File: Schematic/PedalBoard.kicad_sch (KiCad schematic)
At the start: 10 parts, among them U1 SC0918, U2 ADS1115IDGST, U3 ADS1115IDGST, U4 THB001P

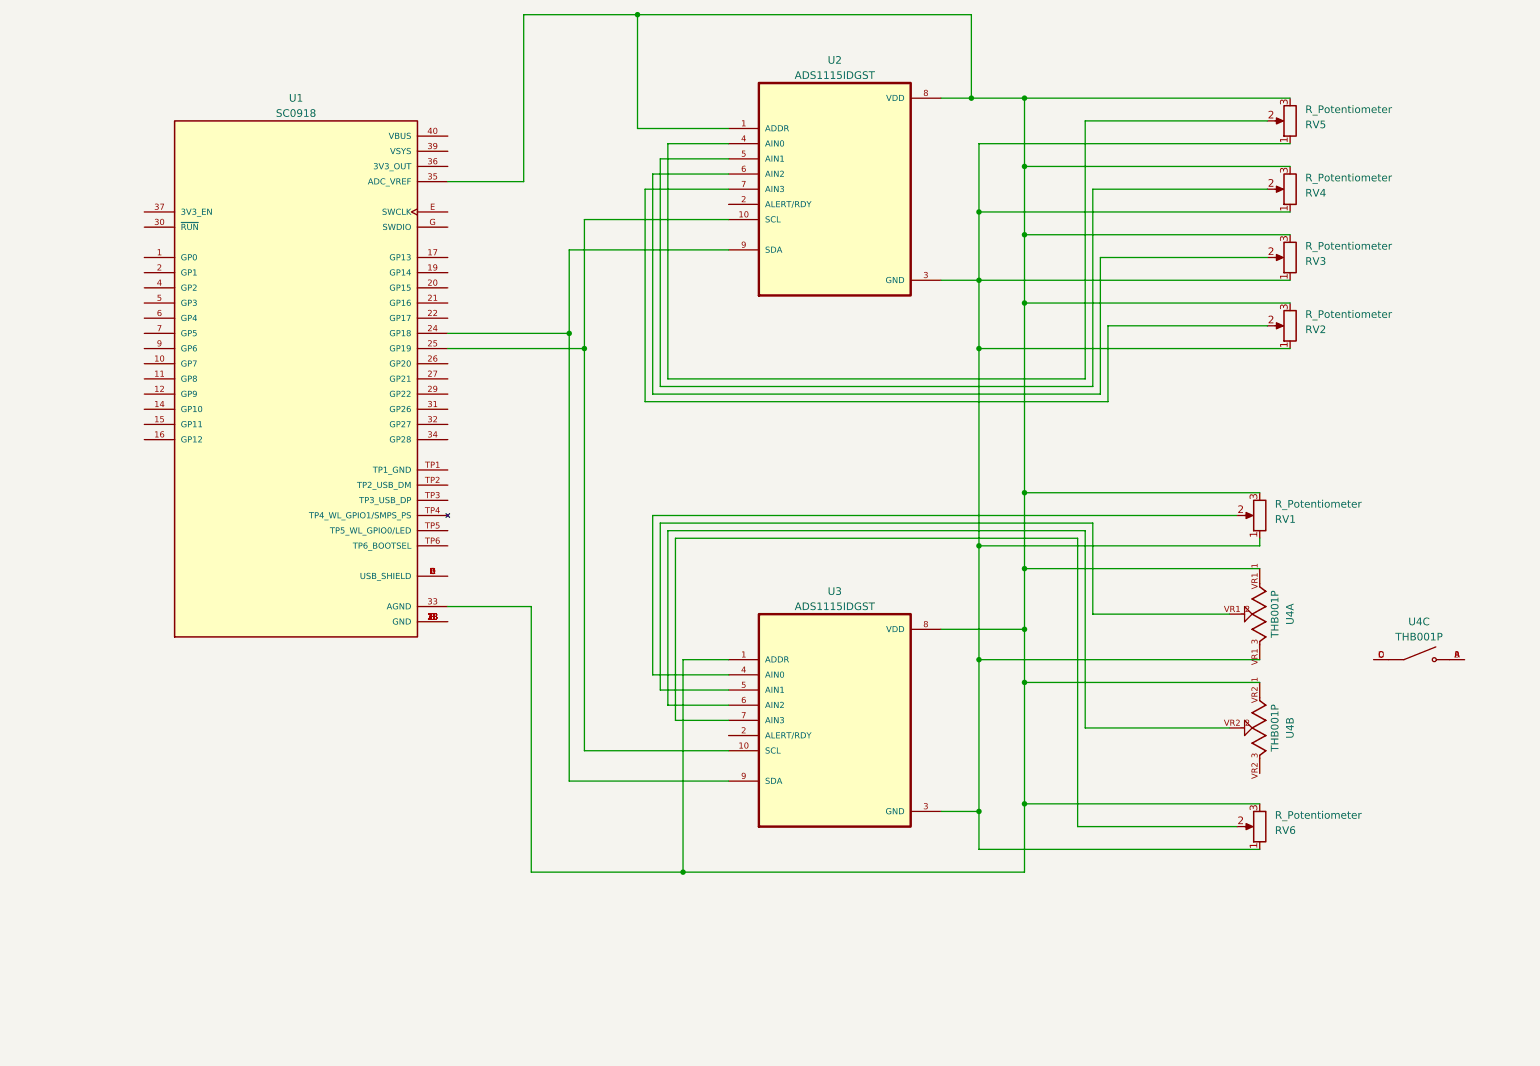
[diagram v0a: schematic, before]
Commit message: Added Leds
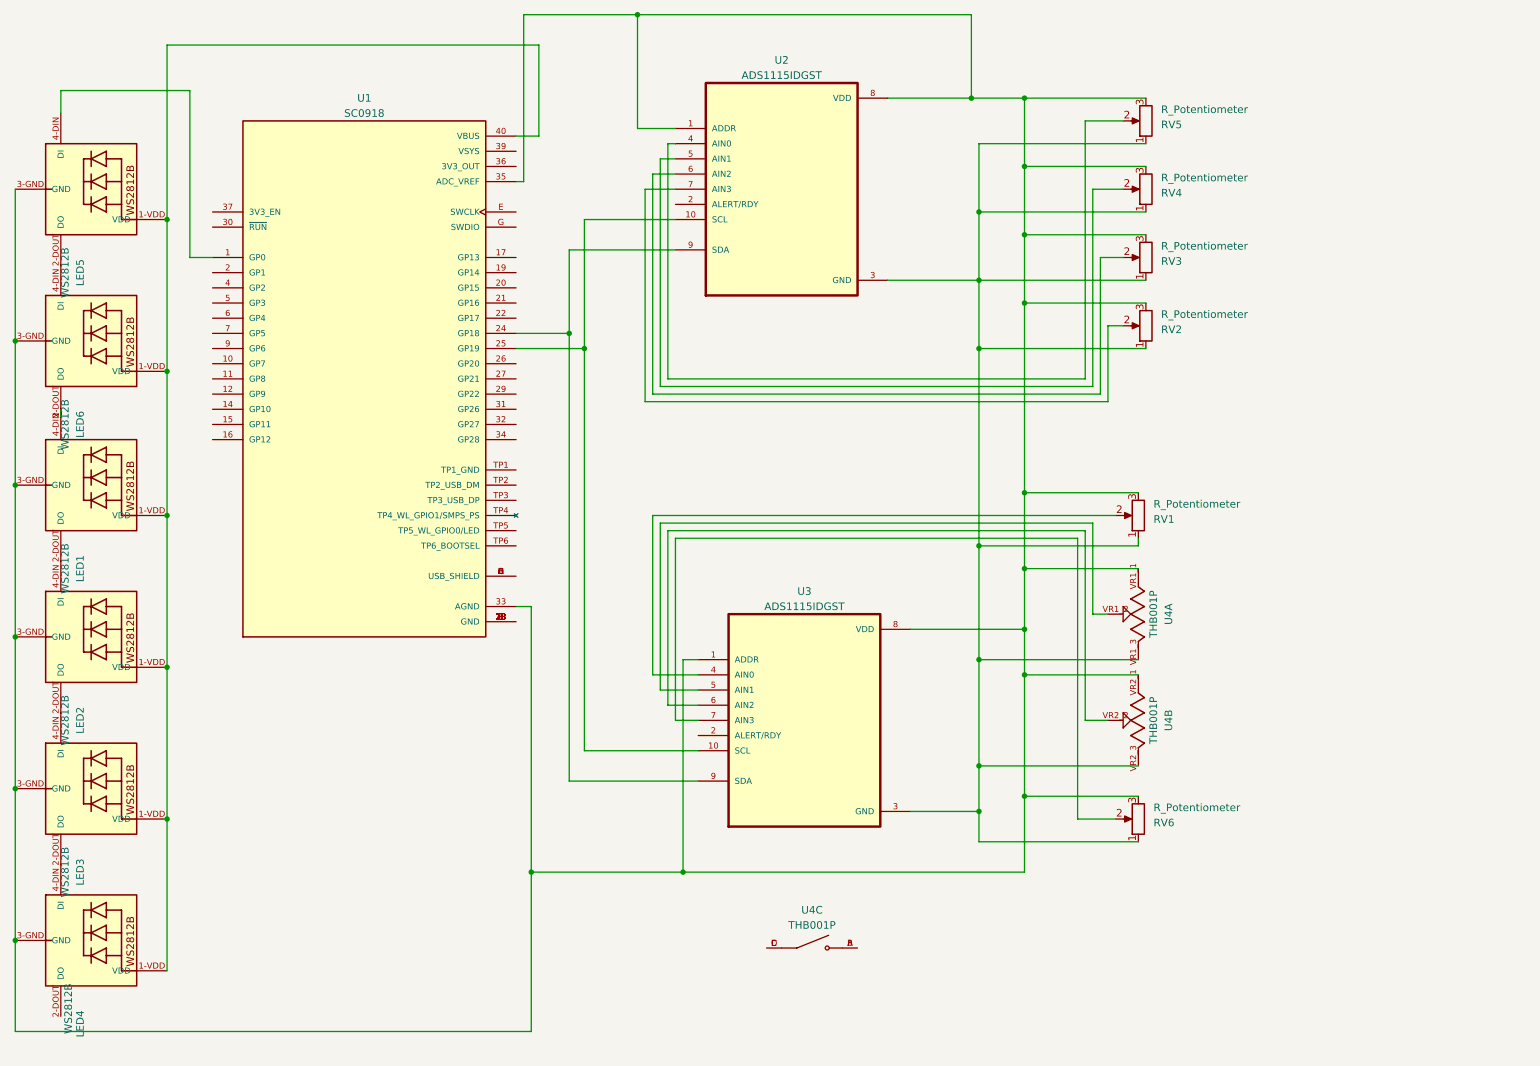
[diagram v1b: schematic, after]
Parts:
- added LED1, LED2, LED3, LED4, LED5, LED6: WS2812B, symbol WS2812B:WS2812B
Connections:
- net at RV1.3, RV2.3, RV3.3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: now also LED1.3-GND (GND), LED2.3-GND (GND), LED3.3-GND (GND), LED4.3-GND (GND), LED5.3-GND (GND), LED6.3-GND (GND)
- net at RV1.1, RV2.1, RV3.1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: now also U4.VR2_3
- net at U1.1 (GP0): now also LED5.4-DIN (DI)
- net at U1.40 (VBUS): now also LED1.1-VDD (VDD), LED2.1-VDD (VDD), LED3.1-VDD (VDD), LED4.1-VDD (VDD), LED5.1-VDD (VDD), LED6.1-VDD (VDD)
- new net: LED5.2-DOUT (DO), LED6.4-DIN (DI)
- new net: LED3.2-DOUT (DO), LED4.4-DIN (DI)
- new net: LED1.2-DOUT (DO), LED2.4-DIN (DI)
- new net: LED1.4-DIN (DI), LED6.2-DOUT (DO)
- new net: LED2.2-DOUT (DO), LED3.4-DIN (DI)
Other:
- moved on the sheet: RV1, RV2, RV3, RV4, RV5, RV6, U1, U2, U3, U4A, U4B, U4C

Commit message: Added footswitch to schematic
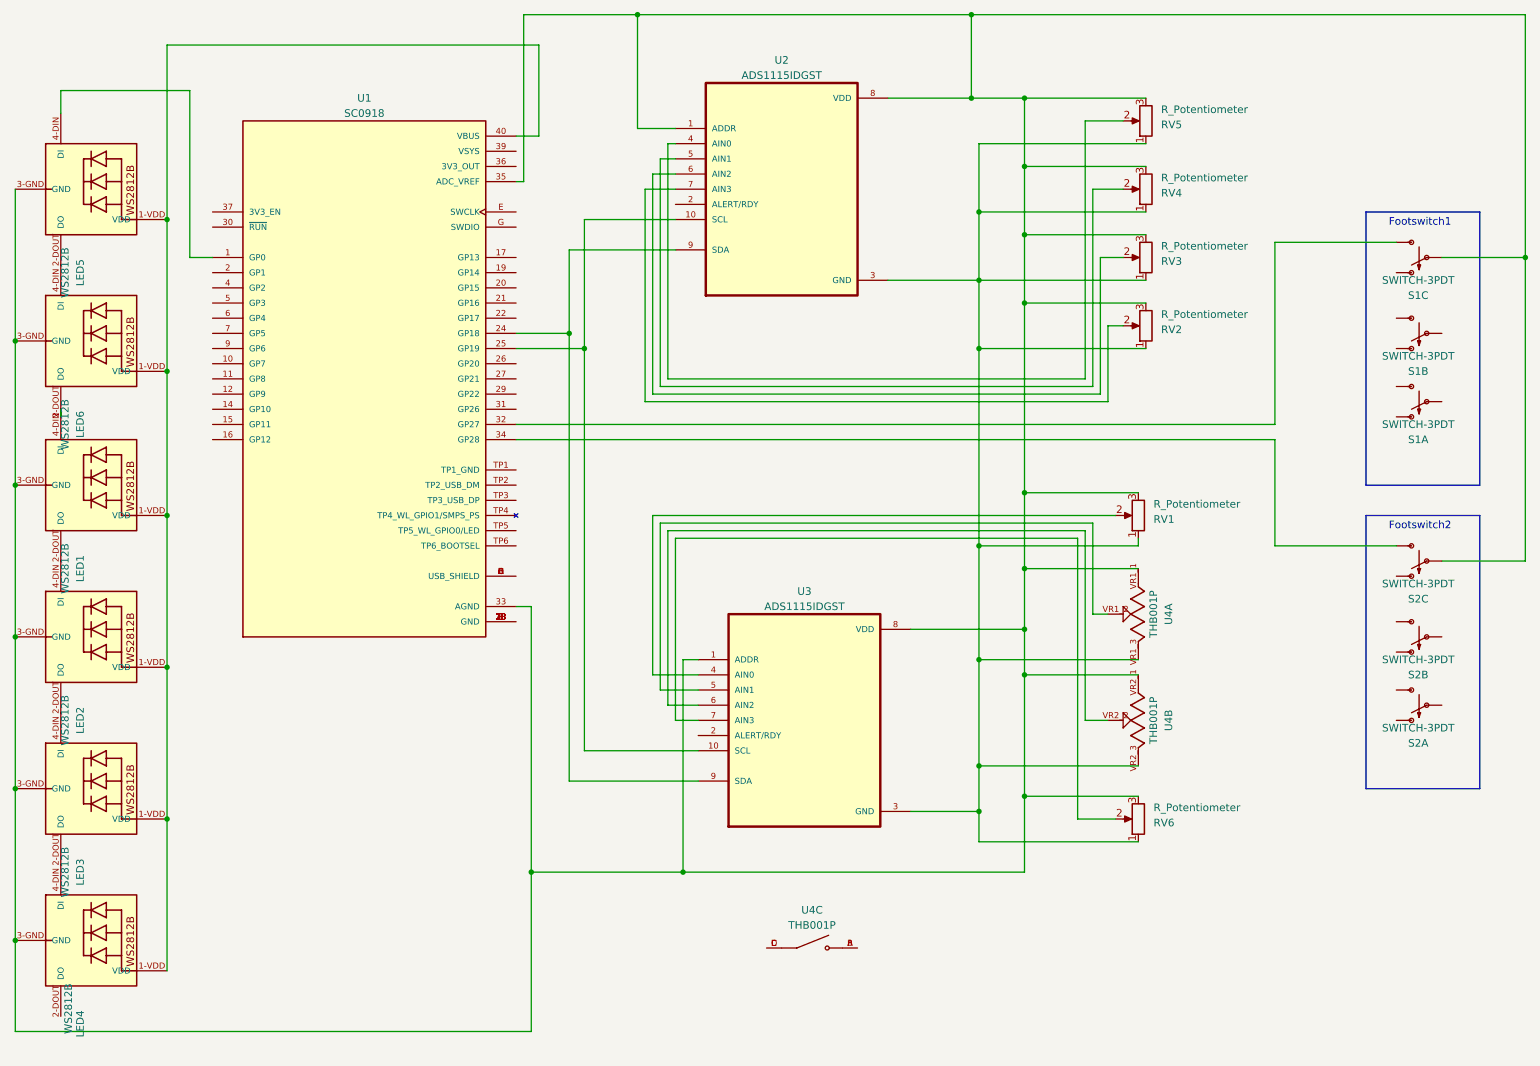
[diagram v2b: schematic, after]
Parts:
- added S1, S2: SWITCH-3PDT, STOMP-SWITCH-3PDT, symbol SparkFun-Electromechanical:SWITCH-3PDT
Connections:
- net at LED1.3-GND (GND), LED2.3-GND (GND), LED3.3-GND (GND)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: now also S1.P$8 (P), S2.P$8 (P)
- net at U1.32 (GP27): now also S1.P$9 (S)
- net at U1.34 (GP28): now also S2.P$9 (S)
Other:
- note added: "Footswitch1"
- note added: "Footswitch2"
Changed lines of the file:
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@@
   (junction (at 191.77 45.72) (diameter 0) (color 0 0 0 0)
   )
+  (junction (at 182.88 20.32) (diameter 0) (color 0 0 0 0)
+  )
   (junction (at 22.86 99.06) (diameter 0) (color 0 0 0 0)
   )
@@
   (junction (at 184.15 53.34) (diameter 0) (color 0 0 0 0)
   )
+  (junction (at 275.59 60.96) (diameter 0) (color 0 0 0 0)
+  )
   (wire (pts (xy 191.77 34.29) (xy 212.09 34.29))
     (stroke (width 0) (type default))
@@
     (stroke (width 0) (type default))
   )
+  (wire (pts (xy 275.59 20.32) (xy 275.59 60.96))
+    (stroke (width 0) (type default))
+  )
   (wire (pts (xy 172.72 153.67) (xy 184.15 153.67))
     (stroke (width 0) (type default))
   )
+  (wire (pts (xy 233.68 91.44) (xy 106.68 91.44))
+    (stroke (width 0) (type default))
+  )
   (wire (pts (xy 200.66 107.95) (xy 200.66 154.94))
     (stroke (width 0) (type default))
@@
     (stroke (width 0) (type default))
   )
+  (wire (pts (xy 233.68 88.9) (xy 106.68 88.9))
+    (stroke (width 0) (type default))
+  )
+  (wire (pts (xy 233.68 109.22) (xy 233.68 91.44))
+    (stroke (width 0) (type default))
+  )
   (wire (pts (xy 191.77 130.81) (xy 210.82 130.81))
     (stroke (width 0) (type default))
@@
     (stroke (width 0) (type default))
   )
+  (wire (pts (xy 182.88 20.32) (xy 275.59 20.32))
+    (stroke (width 0) (type default))
+  )
   (wire (pts (xy 106.68 40.64) (xy 110.49 40.64))
     (stroke (width 0) (type default))
@@
     (stroke (width 0) (type default))
   )
+  (wire (pts (xy 254 109.22) (xy 233.68 109.22))
+    (stroke (width 0) (type default))
+  )
   (wire (pts (xy 184.15 64.77) (xy 168.91 64.77))
     (stroke (width 0) (type default))
@@
     (stroke (width 0) (type default))
   )
+  (wire (pts (xy 275.59 60.96) (xy 261.62 60.96))
+    (stroke (width 0) (type default))
+  )
   (wire (pts (xy 184.15 64.77) (xy 184.15 53.34))
     (stroke (width 0) (type default))
@@
     (stroke (width 0) (type default))
   )
+  (wire (pts (xy 254 58.42) (xy 233.68 58.42))
+    (stroke (width 0) (type default))
+  )
   (wire (pts (xy 130.81 105.41) (xy 130.81 133.35))
     (stroke (width 0) (type default))
@@
     (stroke (width 0) (type default))
   )
+  (wire (pts (xy 233.68 58.42) (xy 233.68 88.9))
+    (stroke (width 0) (type default))
+  )
   (wire (pts (xy 132.08 81.28) (xy 132.08 41.91))
     (stroke (width 0) (type default))
@@
     (stroke (width 0) (type default))
   )
+  (wire (pts (xy 275.59 111.76) (xy 261.62 111.76))
+    (stroke (width 0) (type default))
+  )
   (wire (pts (xy 191.77 68.58) (xy 191.77 57.15))
     (stroke (width 0) (type default))
@@
     (stroke (width 0) (type default))
   )
+  (wire (pts (xy 275.59 60.96) (xy 275.59 111.76))
+    (stroke (width 0) (type default))
+  )
   (wire (pts (xy 48.26 129.54) (xy 48.26 154.94))
     (stroke (width 0) (type default))
@@
   (wire (pts (xy 118.11 143.51) (xy 118.11 76.2))
     (stroke (width 0) (type default))
+  )
+  (rectangle (start 248.92 104.14) (end 267.97 149.86)
+    (stroke (width 0) (type default))
+    (fill (type none))
+  )
+  (rectangle (start 248.92 53.34) (end 267.97 99.06)
+    (stroke (width 0) (type default))
+    (fill (type none))
+  )
+  (text "Footswitch2" (at 252.73 106.68 0)
+    (effects (font (size 1.27 1.27)) (justify left bottom))
+  )
+  (text "Footswitch1\n" (at 252.73 55.88 0)
+    (effects (font (size 1.27 1.27)) (justify left bottom))
   )
   (symbol (lib_id "ADS1115IDGST:ADS1115IDGST") (at 151.13 49.53 0) (unit 1)
@@
     )
   )
+  (symbol (lib_id "SparkFun-Electromechanical:SWITCH-3PDT") (at 256.54 135.89 180) (unit 1)
+    (in_bom yes) (on_board yes) (dnp no) (fields_autoplaced)
+    (property "Reference" "S2" (at 257.6703 142.24 0)
+      (effects (font (size 1.27 1.27)))
+    )
+    (property "Value" "SWITCH-3PDT" (at 257.6703 139.7 0)
+      (effects (font (size 1.27 1.27)))
+    )
+    (property "Footprint" "STOMP-SWITCH-3PDT" (at 255.778 139.7 0)
+      (effects (font (size 0.508 0.508)) hide)
+    )
+    (property "Datasheet" "" (at 256.54 135.89 0)
+      (effects (font (size 1.27 1.27)) hide)
+    )
+    (pin "P$1")
+    (pin "P$2")
+    (pin "P$3")
+    (pin "P$4")
+    (pin "P$5")
+    (pin "P$6")
+    (pin "P$7")
+    (pin "P$8")
+    (pin "P$9")
+    (instances
+      (project "PedalBoard"
+        (path "/8cf0b462-836f-4472-b9dc-73e3a9fbfae5"
+          (reference "S2") (unit 1)
+        )
+      )
+    )
+  )
   (symbol (lib_id "THB001P:THB001P") (at 156.21 176.53 0) (unit 3)
     (in_bom yes) (on_board yes) (dnp no) (fields_autoplaced)
@@
     )
   )
+  (symbol (lib_id "SparkFun-Electromechanical:SWITCH-3PDT") (at 256.54 85.09 180) (unit 1)
+    (in_bom yes) (on_board yes) (dnp no) (fields_autoplaced)
+    (property "Reference" "S1" (at 257.6703 91.44 0)
+      (effects (font (size 1.27 1.27)))
+    )
+    (property "Value" "SWITCH-3PDT" (at 257.6703 88.9 0)
+      (effects (font (size 1.27 1.27)))
+    )
+    (property "Footprint" "STOMP-SWITCH-3PDT" (at 255.778 88.9 0)
+      (effects (font (size 0.508 0.508)) hide)
+    )
+    (property "Datasheet" "" (at 256.54 85.09 0)
+      (effects (font (size 1.27 1.27)) hide)
+    )
+    (pin "P$1")
+    (pin "P$2")
+    (pin "P$3")
+    (pin "P$4")
+    (pin "P$5")
+    (pin "P$6")
+    (pin "P$7")
+    (pin "P$8")
+    (pin "P$9")
+    (instances
+      (project "PedalBoard"
+        (path "/8cf0b462-836f-4472-b9dc-73e3a9fbfae5"
+          (reference "S1") (unit 1)
+        )
+      )
+    )
+  )
   (symbol (lib_id "WS2812B:WS2812B") (at 33.02 99.06 270) (unit 1)
     (in_bom yes) (on_board yes) (dnp no) (fields_autoplaced)
@@
     )
   )
+  (symbol (lib_id "SparkFun-Electromechanical:SWITCH-3PDT") (at 256.54 111.76 180) (unit 3)
+    (in_bom yes) (on_board yes) (dnp no) (fields_autoplaced)
+    (property "Reference" "S2" (at 257.6703 118.11 0)
+      (effects (font (size 1.27 1.27)))
+    )
+    (property "Value" "SWITCH-3PDT" (at 257.6703 115.57 0)
+      (effects (font (size 1.27 1.27)))
+    )
+    (property "Footprint" "STOMP-SWITCH-3PDT" (at 255.778 115.57 0)
+      (effects (font (size 0.508 0.508)) hide)
+    )
+    (property "Datasheet" "" (at 256.54 111.76 0)
+      (effects (font (size 1.27 1.27)) hide)
+    )
+    (pin "P$1")
+    (pin "P$2")
+    (pin "P$3")
+    (pin "P$4")
+    (pin "P$5")
+    (pin "P$6")
+    (pin "P$7")
+    (pin "P$8")
+    (pin "P$9")
+    (instances
+      (project "PedalBoard"
+        (path "/8cf0b462-836f-4472-b9dc-73e3a9fbfae5"
+          (reference "S2") (unit 3)
+        )
+      )
+    )
+  )
   (symbol (lib_id "WS2812B:WS2812B") (at 33.02 124.46 270) (unit 1)
     (in_bom yes) (on_board yes) (dnp no) (fields_autoplaced)
@@
         (path "/8cf0b462-836f-4472-b9dc-73e3a9fbfae5"
           (reference "LED2") (unit 1)
+        )
+      )
+    )
+  )
+  (symbol (lib_id "SparkFun-Electromechanical:SWITCH-3PDT") (at 256.54 60.96 180) (unit 3)
+    (in_bom yes) (on_board yes) (dnp no) (fields_autoplaced)
+    (property "Reference" "S1" (at 257.6703 67.31 0)
+      (effects (font (size 1.27 1.27)))
+    )
+    (property "Value" "SWITCH-3PDT" (at 257.6703 64.77 0)
+      (effects (font (size 1.27 1.27)))
+    )
+    (property "Footprint" "STOMP-SWITCH-3PDT" (at 255.778 64.77 0)
+      (effects (font (size 0.508 0.508)) hide)
+    )
+    (property "Datasheet" "" (at 256.54 60.96 0)
+      (effects (font (size 1.27 1.27)) hide)
+    )
+    (pin "P$1")
+    (pin "P$2")
+    (pin "P$3")
+    (pin "P$4")
+    (pin "P$5")
+    (pin "P$6")
+    (pin "P$7")
+    (pin "P$8")
+    (pin "P$9")
+    (instances
+      (project "PedalBoard"
+        (path "/8cf0b462-836f-4472-b9dc-73e3a9fbfae5"
+          (reference "S1") (unit 3)
         )
       )
@@
     )
   )
+  (symbol (lib_id "SparkFun-Electromechanical:SWITCH-3PDT") (at 256.54 124.46 180) (unit 2)
+    (in_bom yes) (on_board yes) (dnp no) (fields_autoplaced)
+    (property "Reference" "S2" (at 257.6703 130.81 0)
+      (effects (font (size 1.27 1.27)))
+    )
+    (property "Value" "SWITCH-3PDT" (at 257.6703 128.27 0)
+      (effects (font (size 1.27 1.27)))
+    )
+    (property "Footprint" "STOMP-SWITCH-3PDT" (at 255.778 128.27 0)
+      (effects (font (size 0.508 0.508)) hide)
+    )
+    (property "Datasheet" "" (at 256.54 124.46 0)
+      (effects (font (size 1.27 1.27)) hide)
+    )
+    (pin "P$1")
+    (pin "P$2")
+    (pin "P$3")
+    (pin "P$4")
+    (pin "P$5")
+    (pin "P$6")
+    (pin "P$7")
+    (pin "P$8")
+    (pin "P$9")
+    (instances
+      (project "PedalBoard"
+        (path "/8cf0b462-836f-4472-b9dc-73e3a9fbfae5"
+          (reference "S2") (unit 2)
+        )
+      )
+    )
+  )
   (symbol (lib_id "ADS1115IDGST:ADS1115IDGST") (at 154.94 138.43 0) (unit 1)
     (in_bom yes) (on_board yes) (dnp no) (fields_autoplaced)
@@
         )
       )
+    )
+  )
+  (symbol (lib_id "SparkFun-Electromechanical:SWITCH-3PDT") (at 256.54 73.66 180) (unit 2)
+    (in_bom yes) (on_board yes) (dnp no) (fields_autoplaced)
+    (property "Reference" "S1" (at 257.6703 80.01 0)
+      (effects (font (size 1.27 1.27)))
+    )
+    (property "Value" "SWITCH-3PDT" (at 257.6703 77.47 0)
+      (effects (font (size 1.27 1.27)))
+    )
+    (property "Footprint" "STOMP-SWITCH-3PDT" (at 255.778 77.47 0)
+      (effects (font (size 0.508 0.508)) hide)
+    )
+    (property "Datasheet" "" (at 256.54 73.66 0)
+      (effects (font (size 1.27 1.27)) hide)
+    )
+    (pin "P$1")
+    (pin "P$2")
+    (pin "P$3")
+    (pin "P$4")
+    (pin "P$5")
+    (pin "P$6")
+    (pin "P$7")
+    (pin "P$8")
+    (pin "P$9")
+    (instances
+      (project "PedalBoard"
+        (path "/8cf0b462-836f-4472-b9dc-73e3a9fbfae5"
+          (reference "S1") (unit 2)
+        )
+      )
